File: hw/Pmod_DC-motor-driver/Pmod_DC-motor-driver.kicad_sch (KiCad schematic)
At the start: 15 parts, among them J6 Conn_02x06_Odd_Even, J8 Encoder, U1 DRV8833

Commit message: GND
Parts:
- J6: footprint Connector_PinSocket_2.54mm:PinSocket_2x06_P2.54mm_Horizontal -> Connector_PinHeader_2.54mm:PinHeader_2x06_P2.54mm_Horizontal
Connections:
- net 5V is gone; now on net +5V: JP4.2 (B)
- net ENC_A1: now also J8.3 (Pin_3); no longer J8.4 (Pin_4)
- net ENC_B1: now also J8.4 (Pin_4); no longer J8.3 (Pin_3)
- net GND: now also J8.5 (Pin_5); no longer J8.2 (Pin_2)
- net at J8.5 (Pin_5), JP4.1 (A): now also J8.2 (Pin_2); no longer J8.5 (Pin_5)
- net at U1.2 (AOUT1): now also J8.6 (Pin_6); no longer J8.1 (Pin_1)
- net at U1.4 (AOUT2): now also J8.1 (Pin_1); no longer J8.6 (Pin_6)
- net at U1.5 (BOUT2): now also J8.6 (Pin_6); no longer J8.1 (Pin_1)
- net at U1.7 (BOUT1): now also J8.1 (Pin_1); no longer J8.6 (Pin_6)
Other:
- moved on the sheet: C33

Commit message: PCB
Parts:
- added C5: 10u, Capacitor_SMD:C_0603_1608Metric, symbol Device:C
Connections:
- net +5V: now also C5.1
- net GND: now also C5.2
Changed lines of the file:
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@@
   (junction (at 162.56 78.74) (diameter 0) (color 0 0 0 0)
   )
-  (junction (at 139.7 76.2) (diameter 0) (color 0 0 0 0)
+  (junction (at 129.54 76.2) (diameter 0) (color 0 0 0 0)
   )
   (junction (at 205.74 101.6) (diameter 0) (color 0 0 0 0)
@@
   (junction (at 50.8 91.44) (diameter 0) (color 0 0 0 0)
   )
+  (junction (at 129.54 78.74) (diameter 0) (color 0 0 0 0)
+  )
   (junction (at 238.76 60.96) (diameter 0) (color 0 0 0 0)
   )
@@
     (stroke (width 0) (type default))
   )
-  (wire (pts (xy 139.7 76.2) (xy 170.18 76.2))
-    (stroke (width 0) (type default))
-  )
   (wire (pts (xy 243.84 68.58) (xy 241.3 68.58))
     (stroke (width 0) (type default))
@@
     (stroke (width 0) (type default))
   )
-  (wire (pts (xy 139.7 73.66) (xy 139.7 76.2))
+  (wire (pts (xy 129.54 73.66) (xy 129.54 76.2))
     (stroke (width 0) (type default))
   )
@@
     (stroke (width 0) (type default))
   )
-  (wire (pts (xy 139.7 76.2) (xy 139.7 78.74))
+  (wire (pts (xy 129.54 76.2) (xy 129.54 78.74))
+    (stroke (width 0) (type default))
+  )
+  (wire (pts (xy 129.54 95.25) (xy 129.54 88.9))
     (stroke (width 0) (type default))
   )
@@
     (stroke (width 0) (type default))
   )
+  (wire (pts (xy 129.54 78.74) (xy 139.7 78.74))
+    (stroke (width 0) (type default))
+  )
+  (wire (pts (xy 129.54 76.2) (xy 170.18 76.2))
+    (stroke (width 0) (type default))
+  )
   (wire (pts (xy 162.56 96.52) (xy 162.56 99.06))
     (stroke (width 0) (type default))
@@
   )
   (wire (pts (xy 139.7 78.74) (xy 139.7 81.28))
+    (stroke (width 0) (type default))
+  )
+  (wire (pts (xy 129.54 78.74) (xy 129.54 81.28))
     (stroke (width 0) (type default))
   )
@@
         (path "/85016b2a-c49e-4d19-83e7-d6dc6b01fcd5"
           (reference "C33") (unit 1)
+        )
+      )
+    )
+  )
+  (symbol (lib_id "power:GND") (at 129.54 95.25 0) (unit 1)
+    (in_bom yes) (on_board yes) (dnp no) (fields_autoplaced)
+    (property "Reference" "#PWR014" (at 129.54 101.6 0)
+      (effects (font (size 1.27 1.27)) hide)
+    )
+    (property "Value" "GND" (at 129.54 100.33 0)
+      (effects (font (size 1.27 1.27)))
+    )
+    (property "Footprint" "" (at 129.54 95.25 0)
+      (effects (font (size 1.27 1.27)) hide)
+    )
+    (property "Datasheet" "" (at 129.54 95.25 0)
+      (effects (font (size 1.27 1.27)) hide)
+    )
+    (pin "1")
+    (instances
+      (project "Pmod_DC-motor-driver"
+        (path "/0d71389d-6b73-4843-8c44-c08bb4c79eb7"
+          (reference "#PWR014") (unit 1)
         )
       )
@@
     )
   )
-  (symbol (lib_id "power:+5V") (at 139.7 73.66 0) (unit 1)
-    (in_bom yes) (on_board yes) (dnp no) (fields_autoplaced)
-    (property "Reference" "#PWR01" (at 139.7 77.47 0)
-      (effects (font (size 1.27 1.27)) hide)
-    )
-    (property "Value" "+5V" (at 139.7 68.58 0)
-      (effects (font (size 1.27 1.27)))
-    )
-    (property "Footprint" "" (at 139.7 73.66 0)
-      (effects (font (size 1.27 1.27)) hide)
-    )
-    (property "Datasheet" "" (at 139.7 73.66 0)
+  (symbol (lib_id "power:+5V") (at 129.54 73.66 0) (unit 1)
+    (in_bom yes) (on_board yes) (dnp no) (fields_autoplaced)
+    (property "Reference" "#PWR01" (at 129.54 77.47 0)
+      (effects (font (size 1.27 1.27)) hide)
+    )
+    (property "Value" "+5V" (at 129.54 68.58 0)
+      (effects (font (size 1.27 1.27)))
+    )
+    (property "Footprint" "" (at 129.54 73.66 0)
+      (effects (font (size 1.27 1.27)) hide)
+    )
+    (property "Datasheet" "" (at 129.54 73.66 0)
       (effects (font (size 1.27 1.27)) hide)
     )
@@
         )
       )
+    )
+  )
+  (symbol (lib_id "Device:C") (at 129.54 85.09 0) (unit 1)
+    (in_bom yes) (on_board yes) (dnp no) (fields_autoplaced)
+    (property "Reference" "C5" (at 133.35 83.82 0)
+      (effects (font (size 1.27 1.27)) (justify left))
+    )
+    (property "Value" "10u" (at 133.35 86.36 0)
+      (effects (font (size 1.27 1.27)) (justify left))
+    )
+    (property "Footprint" "Capacitor_SMD:C_0603_1608Metric" (at 130.5052 88.9 0)
+      (effects (font (size 1.27 1.27)) hide)
+    )
+    (property "Datasheet" "~" (at 129.54 85.09 0)
+      (effects (font (size 1.27 1.27)) hide)
+    )
+    (property "Basic/Extended" "B" (at 129.54 85.09 0)
+      (effects (font (size 1.27 1.27)) hide)
+    )
+    (property "LCSC" "C96446" (at 129.54 85.09 0)
+      (effects (font (size 1.27 1.27)) hide)
+    )
+    (property "info" "25V, X5R" (at 129.54 85.09 0)
+      (effects (font (size 1.27 1.27)) hide)
+    )
+    (pin "1")
+    (pin "2")
+    (instances
+      (project "Zelvicka"
+        (path "/04d53a73-373f-40ca-9ff1-406e2f105d42/30180d4c-33b6-4015-8bb1-ca093d0ad03d"
+          (reference "C5") (unit 1)
+        )
+      )
+      (project "Pmod_DC-motor-driver"
+        (path "/0d71389d-6b73-4843-8c44-c08bb4c79eb7"
+          (reference "C1") (unit 1)
+        )
+      )
+      (project "motor_control"
+        (path "/85016b2a-c49e-4d19-83e7-d6dc6b01fcd5"
+          (reference "C5") (unit 1)
+        )
+      )

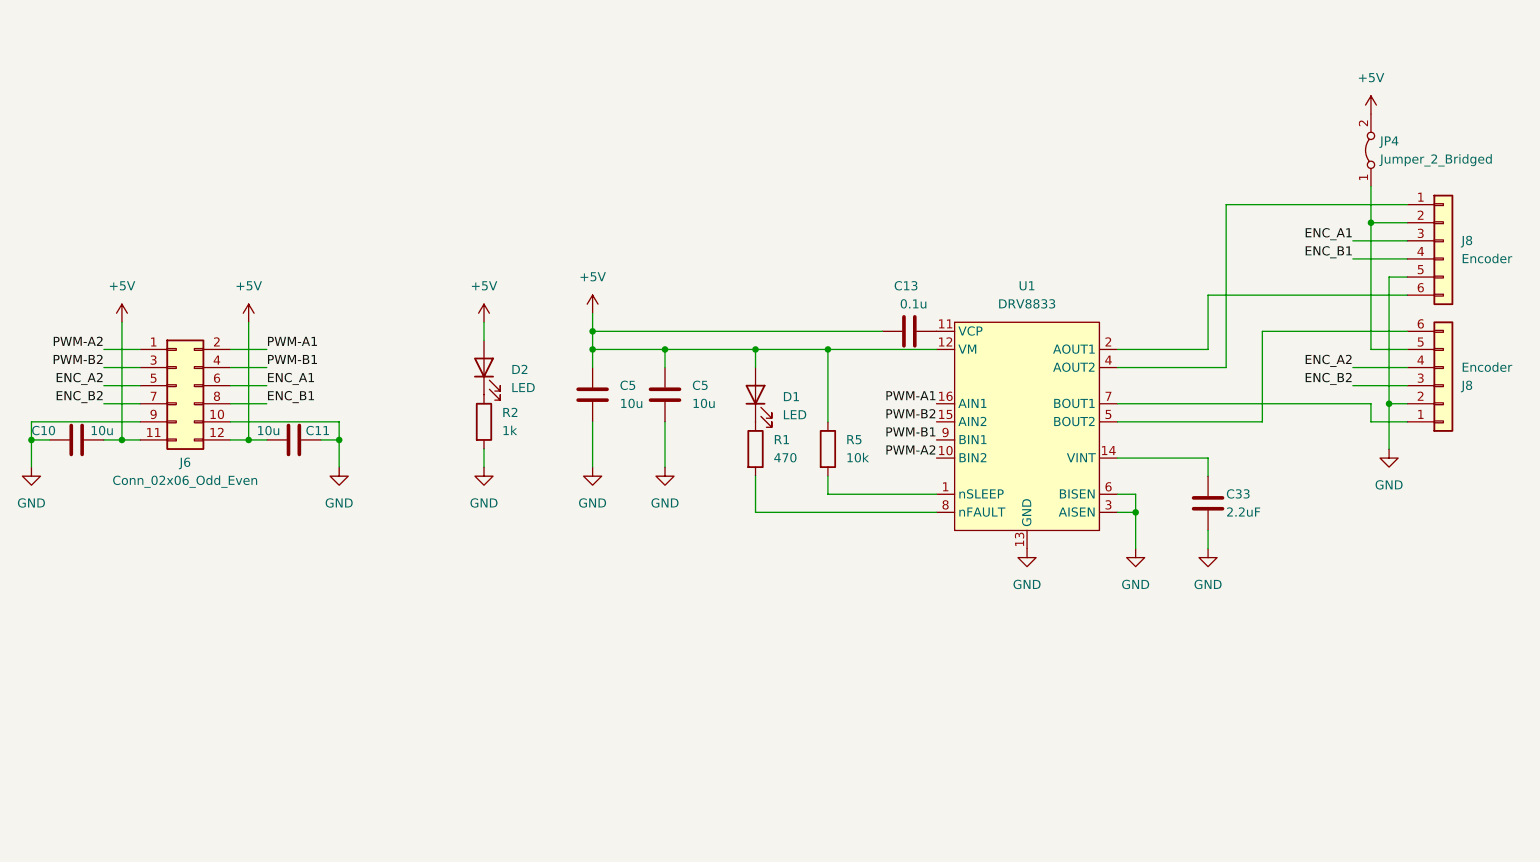
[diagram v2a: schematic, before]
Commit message: Add divider to ENC line
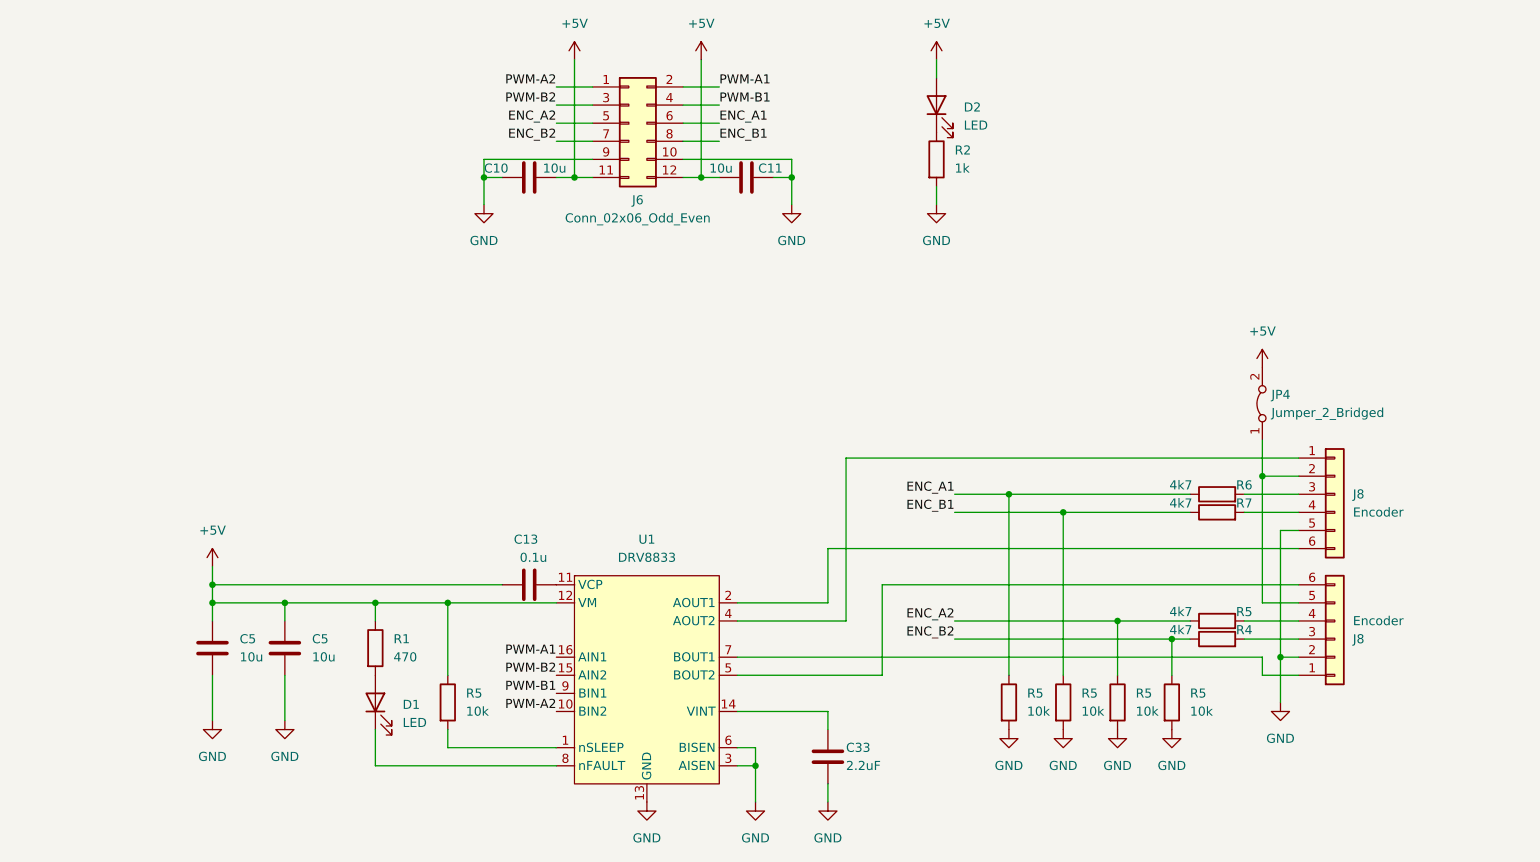
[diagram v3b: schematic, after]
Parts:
- added R4, R5, R6, R7: 4k7, Resistor_SMD:R_0402_1005Metric, symbol Device:R
- added R5 (x4): 10k, Resistor_SMD:R_0402_1005Metric, symbol Device:R
- R5: footprint Resistor_SMD:R_0603_1608Metric -> Resistor_SMD:R_0402_1005Metric; LCSC C25804 -> C25744
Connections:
- net +5V: now also R1.1; no longer D1.2 (A)
- net ENC_A1: now also R5.1, R6.1; no longer J8.3 (Pin_3)
- net ENC_A2: now also R5.1, R5.1; no longer J8.4 (Pin_4)
- net ENC_B1: now also R5.1, R7.1; no longer J8.4 (Pin_4)
- net ENC_B2: now also R4.1, R5.1; no longer J8.3 (Pin_3)
- net GND: now also R5.2, R5.2, R5.2, R5.2
- net at D1.1 (K): now also U1.8 (nFAULT); no longer R1.1
- net at R1.2: now also D1.2 (A); no longer U1.8 (nFAULT)
- new net: J8.4 (Pin_4), R7.2
- new net: J8.3 (Pin_3), R6.2
- new net: J8.4 (Pin_4), R5.2
- new net: J8.3 (Pin_3), R4.2
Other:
- moved on the sheet: C10, C11, C13, C33, C5, D1, D2, J6, J8, JP4, R1, R2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
